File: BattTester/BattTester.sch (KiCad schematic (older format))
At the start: 25 parts, among them J1 Battery, J2 SD_Card, J3 PWR, J4 UPDI, Q1 IRLZ44N, U1 LTC1286CN8, U2 ATtiny1624-SS, U3 LD1086DT33, U4 LM358AN

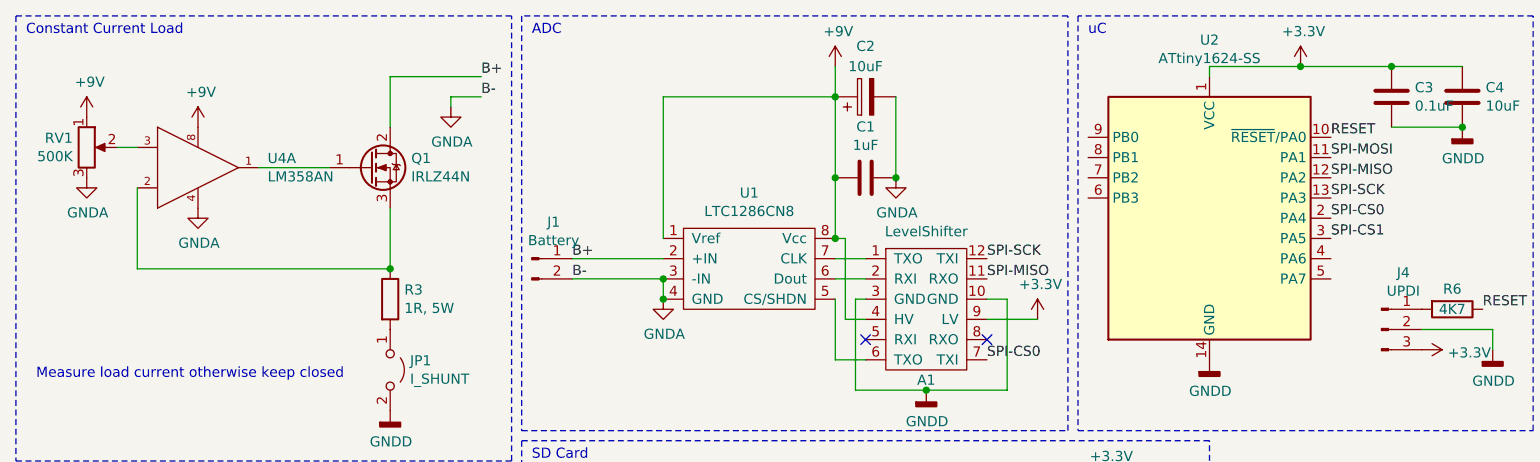
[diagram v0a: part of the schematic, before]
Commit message: cutoff mosfet and higher power Rload
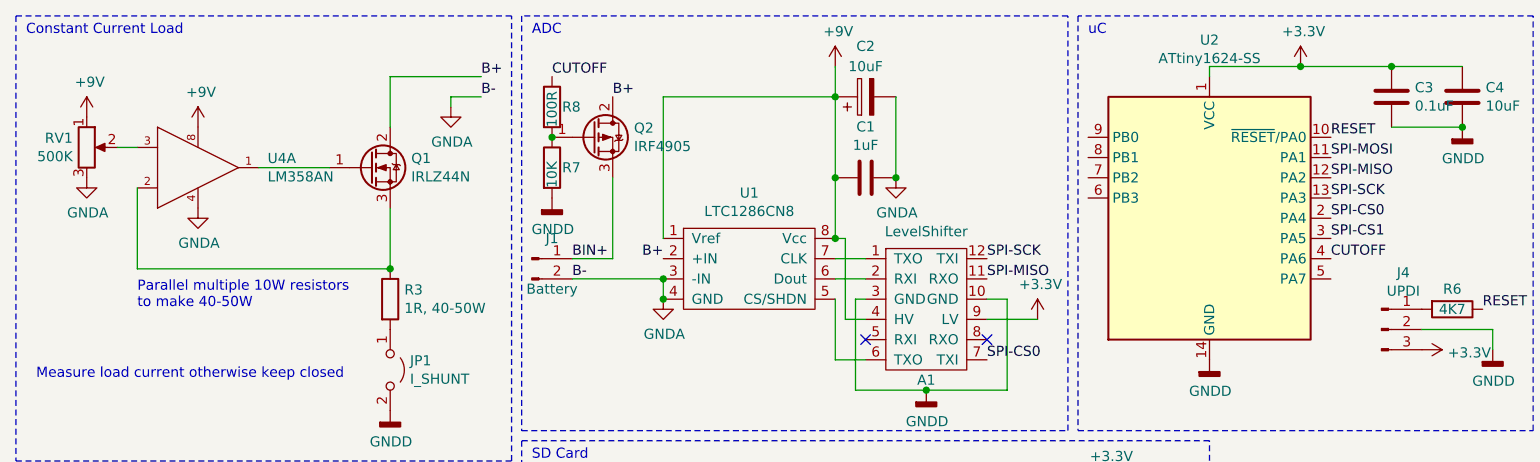
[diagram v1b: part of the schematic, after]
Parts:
- added Q2: IRF4905, Package_TO_SOT_THT:TO-220-3_Vertical, symbol Transistor_FET:IRF4905
- added R7: 10K, Resistor_SMD:R_1206_3216Metric_Pad1.30x1.75mm_HandSolder, symbol Device:R
- added R8: 100R, Resistor_SMD:R_1206_3216Metric_Pad1.30x1.75mm_HandSolder, symbol Device:R
- R3: value 1R, 5W -> 1R, 40-50W; footprint Resistor_THT:R_Axial_Power_L48.0mm_W12.5mm_P55.88mm -> BattTester:10xParallel_R_Axial_DIN0614_L14.3mm_D5.7mm_P15.24mm_Horizontal
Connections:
- net B+: now also Q2.2 (D); no longer J1.1 (Pin_1)
- net GND: now also R7.2
- net CUTOFF: now reaches U2.4 (PA6)
- net CUTOFF: now also R8.1
- new net: Q2.1 (G), R7.1, R8.2
- new net BIN+: J1.1 (Pin_1), Q2.3 (S)
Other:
- note added: "Parallel multiple 10W resistors \nto make 40-50W\n"
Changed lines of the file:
@@
 U 1 1 616C4F2E
 P 3050 1700
-F 0 "J1" H 3158 1881 50  0000 C CNN
-F 1 "Battery" H 3158 1790 50  0000 C CNN
+F 0 "J1" H 3150 1800 50  0000 C CNN
+F 1 "Battery" H 3150 1550 50  0000 C CNN
 F 2 "Connector_PinHeader_2.54mm:PinHeader_1x02_P2.54mm_Vertical" H 3050 1700 50  0001 C CNN
 F 3 "~" H 3050 1700 50  0001 C CNN
 	1    3050 1700
-	1    0    0    -1
-$EndComp
-$Comp
-L power:GNDA #PWR0101
-U 1 1 616C6E3A
-P 3700 1900
-F 0 "#PWR0101" H 3700 1650 50  0001 C CNN
-F 1 "GNDA" H 3705 1727 50  0000 C CNN
-F 2 "" H 3700 1900 50  0001 C CNN
-F 3 "" H 3700 1900 50  0001 C CNN
-	1    3700 1900
 	1    0    0    -1
 $EndComp
@@
 	1100 1350 1100 1750
 Wire Wire Line
-	1100 1750 2350 1750
-Wire Wire Line
 	2350 1450 2350 1750
-$Comp
-L Device:R R3
-U 1 1 6173721B
-P 2350 1900
-F 0 "R3" H 2420 1946 50  0000 L CNN
-F 1 "1R, 5W" H 2420 1855 50  0000 L CNN
-F 2 "Resistor_THT:R_Axial_Power_L48.0mm_W12.5mm_P55.88mm" V 2280 1900 50  0001 C CNN
-F 3 "~" H 2350 1900 50  0001 C CNN
-	1    2350 1900
-	1    0    0    -1
-$EndComp
-Connection ~ 2350 1750
 Wire Wire Line
 	2350 1050 2350 800
@@
 Text Label 2800 800  0    50   ~ 0
 B+
-Connection ~ 3700 1900
 Text Label 3250 1800 0    50   ~ 0
 B-
-Text Label 3250 1700 0    50   ~ 0
-B+
 Text Label 2800 900  0    50   ~ 0
 B-
 Wire Wire Line
-	2800 900  2650 900
-Wire Wire Line
-	2650 900  2650 950
-$Comp
-L power:GNDA #PWR0123
-U 1 1 61740EA0
-P 2650 950
-F 0 "#PWR0123" H 2650 700 50  0001 C CNN
-F 1 "GNDA" H 2655 777 50  0000 C CNN
-F 2 "" H 2650 950 50  0001 C CNN
-F 3 "" H 2650 950 50  0001 C CNN
-	1    2650 950
-	1    0    0    -1
-$EndComp
-Wire Wire Line
 	1000 1150 1100 1150
-Wire Wire Line
-	3250 1700 3700 1700
 $Comp
 L BattTester:LT1286CN8 U1
@@
 Wire Wire Line
 	1150 4300 850  4300
-$Comp
-L power:GNDD #PWR0122
-U 1 1 6178CCE3
+Wire Wire Line
+	7800 2050 7450 2050
+Text Label 3700 1700 2    50   ~ 0
+B+
+Connection ~ 3700 1800
+$Comp
+L power:GNDA #PWR0101
+U 1 1 616C6E3A
+P 3700 1900
+F 0 "#PWR0101" H 3700 1650 50  0001 C CNN
+F 1 "GNDA" H 3705 1727 50  0000 C CNN
+F 2 "" H 3700 1900 50  0001 C CNN
+F 3 "" H 3700 1900 50  0001 C CNN
+	1    3700 1900
+	1    0    0    -1
+$EndComp
+Connection ~ 3700 1900
+Wire Wire Line
+	3250 1800 3700 1800
+Wire Wire Line
+	2800 900  2650 900
+Wire Wire Line
+	2650 900  2650 950
+$Comp
+L power:GNDA #PWR0122
+U 1 1 6171593F
+P 2650 950
+F 0 "#PWR0122" H 2650 700 50  0001 C CNN
+F 1 "GNDA" H 2655 777 50  0000 C CNN
+F 2 "" H 2650 950 50  0001 C CNN
+F 3 "" H 2650 950 50  0001 C CNN
+	1    2650 950
+	1    0    0    -1
+$EndComp
+$Comp
+L power:GNDD #PWR0123
+U 1 1 61715D3B
 P 2350 2450
-F 0 "#PWR0122" H 2350 2200 50  0001 C CNN
+F 0 "#PWR0123" H 2350 2200 50  0001 C CNN
 F 1 "GNDD" H 2354 2295 50  0000 C CNN
 F 2 "" H 2350 2450 50  0001 C CNN
@@
 	1    0    0    -1
 $EndComp
-Wire Wire Line
-	7800 2050 7450 2050
-Connection ~ 3700 1800
-Wire Wire Line
-	3250 1800 3700 1800
+$Comp
+L Transistor_FET:IRF4905 Q2
+U 1 1 616DBDAF
+P 3350 1100
+F 0 "Q2" H 3555 1146 50  0000 L CNN
+F 1 "IRF4905" H 3555 1055 50  0000 L CNN
+F 2 "Package_TO_SOT_THT:TO-220-3_Vertical" H 3550 1025 50  0001 L CIN
+F 3 "http://www.infineon.com/dgdl/irf4905.pdf?fileId=5546d462533600a4015355e32165197c" H 3350 1100 50  0001 L CNN
+	1    3350 1100
+	1    0    0    -1
+$EndComp
+Text Label 3450 900  0    50   ~ 0
+B+
+Text Label 3150 800  0    50   ~ 0
+CUTOFF
+Text Label 3250 1700 0    50   ~ 0
+BIN+
+Wire Wire Line
+	3450 1700 3450 1300
+Wire Wire Line
+	3250 1700 3450 1700
+$Comp
+L Device:R R8
+U 1 1 616FC2A8
+P 3150 950
+F 0 "R8" H 3200 950 50  0000 L CNN
+F 1 "100R" V 3150 850 50  0000 L CNN
+F 2 "Resistor_SMD:R_1206_3216Metric_Pad1.30x1.75mm_HandSolder" V 3080 950 50  0001 C CNN
+F 3 "~" H 3150 950 50  0001 C CNN
+	1    3150 950
+	1    0    0    -1
+$EndComp
+$Comp
+L Device:R R7
+U 1 1 616FD045
+P 3150 1250
+F 0 "R7" H 3200 1250 50  0000 L CNN
+F 1 "10K" V 3150 1150 50  0000 L CNN
+F 2 "Resistor_SMD:R_1206_3216Metric_Pad1.30x1.75mm_HandSolder" V 3080 1250 50  0001 C CNN
+F 3 "~" H 3150 1250 50  0001 C CNN
+	1    3150 1250
+	1    0    0    -1
+$EndComp
+Connection ~ 3150 1100
+$Comp
+L power:GNDD #PWR0126
+U 1 1 616FFF6B
+P 3150 1400
+F 0 "#PWR0126" H 3150 1150 50  0001 C CNN
+F 1 "GNDD" H 3154 1245 50  0000 C CNN
+F 2 "" H 3150 1400 50  0001 C CNN
+F 3 "" H 3150 1400 50  0001 C CNN
+	1    3150 1400
+	1    0    0    -1
+$EndComp
+Text Label 7000 1700 0    50   ~ 0
+CUTOFF
+Connection ~ 2350 1750
+Wire Wire Line
+	1100 1750 2350 1750
+$Comp
+L Device:R R3
+U 1 1 6173721B
+P 2350 1900
+F 0 "R3" H 2420 1946 50  0000 L CNN
+F 1 "1R, 40-50W" H 2420 1855 50  0000 L CNN
+F 2 "BattTester:10xParallel_R_Axial_DIN0614_L14.3mm_D5.7mm_P15.24mm_Horizontal" V 2280 1900 50  0001 C CNN
+F 3 "~" H 2350 1900 50  0001 C CNN
+	1    2350 1900
+	1    0    0    -1
+$EndComp
+Text Notes 1100 1950 0    50   ~ 0
+Parallel multiple 10W resistors \nto make 40-50W\n
 $EndSCHEMATC

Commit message: Fix #1
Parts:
- added Q3: 2N7002, Package_TO_SOT_SMD:SOT-23, symbol Transistor_FET:2N7002
- added R9: 10K, Resistor_SMD:R_1206_3216Metric_Pad1.30x1.75mm_HandSolder, symbol Device:R
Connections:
- net BIN+: now also R7.2
- net GND: now also Q3.2 (S), R9.2; no longer R7.2
- net at Q2.1 (G), R7.1: now also Q3.3 (D); no longer R8.2
- new net: Q3.1 (G), R8.2, R9.1
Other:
- moved on the sheet: A1, C1, C2, C3, C4, J1, J4, Q2, R6, R7, R8, U1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

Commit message: current check
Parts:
- added R?: 10m, symbol Device:R
- added R?: 100R, symbol Device:R
- added R?: 2K, symbol Device:R
- added U?: LT6106, Package_TO_SOT_SMD:SOT-23-5, symbol Amplifier_Current:LT6106
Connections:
- net GND: now also R?.2, U?.2 (V-)
- new net: R?.1, U?.3 (-)
- new net: R?.2, U?.4 (+)
- new net: R?.1, R?.2, U?.5 (V+)
- new net I_OUT: R?.1, U?.1
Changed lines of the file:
@@
 	1    0    0    -1
 $EndComp
-Text Label 3300 1700 0    50   ~ 0
-BIN+
 Text Label 3900 800  0    50   ~ 0
 CUTOFF
@@
 Text Label 4200 1700 2    50   ~ 0
 B+
+$Comp
+L Amplifier_Current:LT6106 U?
+U 1 1 61967F7F
+P 7800 3400
+F 0 "U?" H 8144 3446 50  0000 L CNN
+F 1 "LT6106" H 8144 3355 50  0000 L CNN
+F 2 "Package_TO_SOT_SMD:SOT-23-5" H 7800 3400 50  0001 C CNN
+F 3 "https://www.analog.com/media/en/technical-documentation/data-sheets/6106fb.pdf" H 7850 3600 50  0001 C CNN
+	1    7800 3400
+	1    0    0    -1
+$EndComp
+$Comp
+L Device:R R?
+U 1 1 6196A136
+P 6900 3400
+F 0 "R?" H 6950 3400 50  0000 L CNN
+F 1 "10m" V 6900 3300 50  0000 L CNN
+F 2 "" V 6830 3400 50  0001 C CNN
+F 3 "~" H 6900 3400 50  0001 C CNN
+	1    6900 3400
+	1    0    0    -1
+$EndComp
+$Comp
+L Device:R R?
+U 1 1 6196AB0E
+P 7150 3250
+F 0 "R?" V 7050 3250 50  0000 C CNN
+F 1 "100R" V 7150 3250 50  0000 C CNN
+F 2 "" V 7080 3250 50  0001 C CNN
+F 3 "~" H 7150 3250 50  0001 C CNN
+	1    7150 3250
+	0    1    1    0
+$EndComp
+$Comp
+L Device:R R?
+U 1 1 6196BAA8
+P 8100 3550
+F 0 "R?" H 8150 3550 50  0000 L CNN
+F 1 "2K" V 8100 3500 50  0000 L CNN
+F 2 "" V 8030 3550 50  0001 C CNN
+F 3 "~" H 8100 3550 50  0001 C CNN
+	1    8100 3550
+	1    0    0    -1
+$EndComp
+Wire Wire Line
+	6900 3250 7000 3250
+Wire Wire Line
+	6900 3550 7300 3550
+Wire Wire Line
+	7300 3250 7500 3500
+Wire Wire Line
+	7300 3550 7500 3300
+Wire Wire Line
+	7700 3100 6900 3100
+Wire Wire Line
+	6900 3100 6900 3250
+Connection ~ 6900 3250
+$Comp
+L power:GNDD #PWR?
+U 1 1 61978BAC
+P 7700 3700
+F 0 "#PWR?" H 7700 3450 50  0001 C CNN
+F 1 "GNDD" H 7704 3545 50  0000 C CNN
+F 2 "" H 7700 3700 50  0001 C CNN
+F 3 "" H 7700 3700 50  0001 C CNN
+	1    7700 3700
+	1    0    0    -1
+$EndComp
+Wire Wire Line
+	7700 3700 8100 3700
+Connection ~ 7700 3700
+Text Label 8350 3400 0    50   ~ 0
+I_OUT
+Wire Wire Line
+	8100 3400 8350 3400
+Connection ~ 8100 3400
+Text Label 3300 1700 0    50   ~ 0
+BIN+
 $EndSCHEMATC

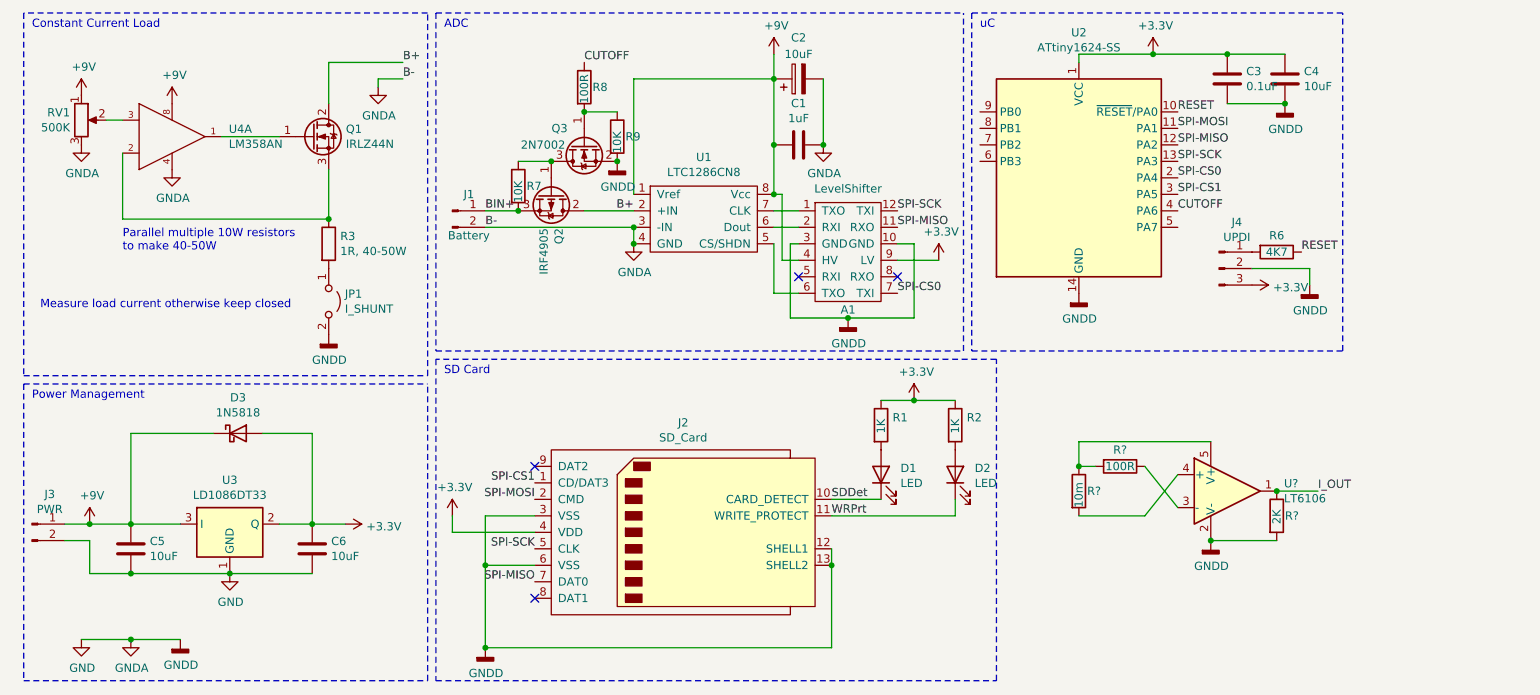
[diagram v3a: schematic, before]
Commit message: add current sense
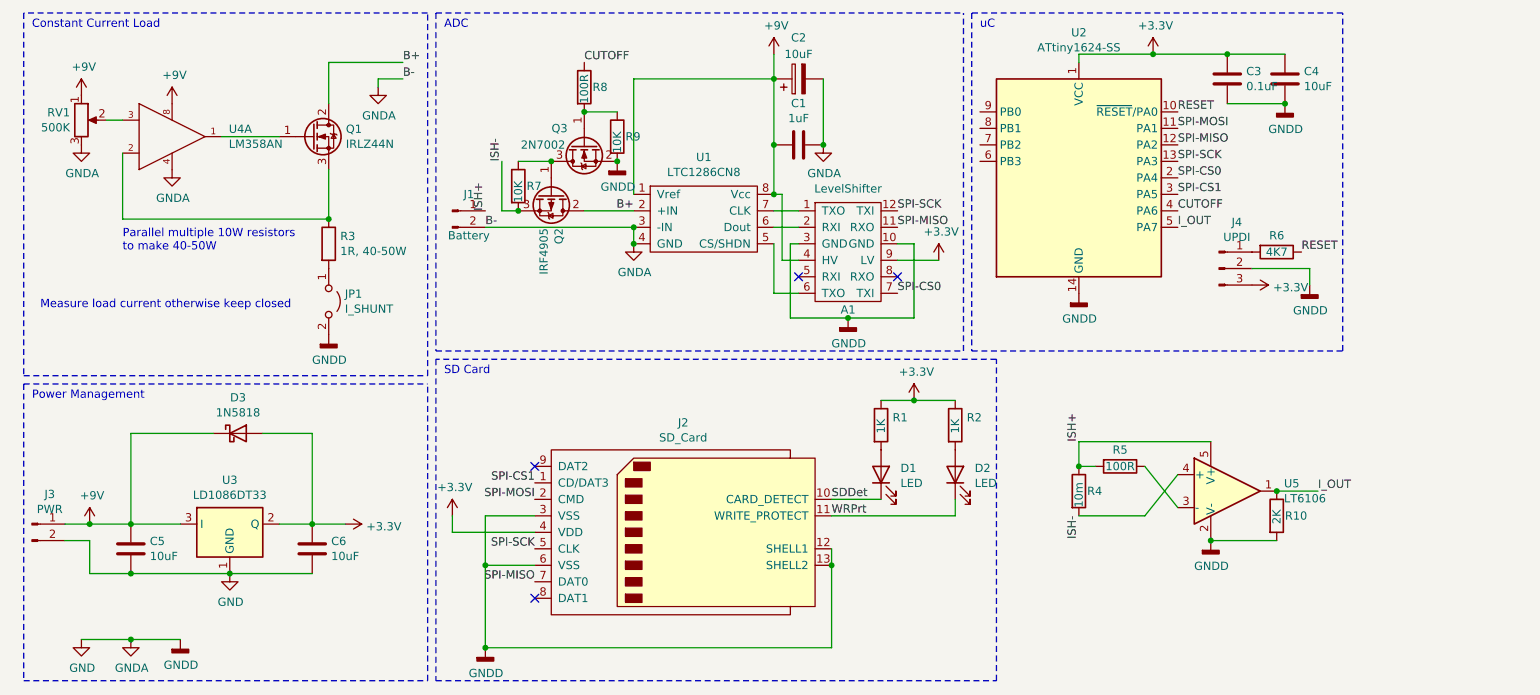
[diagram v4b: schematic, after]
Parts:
- R10, R5: renamed from R?; footprint (none) -> Resistor_SMD:R_0805_2012Metric_Pad1.20x1.40mm_HandSolder
- R4: renamed from R?; footprint (none) -> Resistor_SMD:R_2816_7142Metric_Pad3.20x4.45mm_HandSolder
- gave numbers to parts that had none: 1
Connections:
- net I_OUT: now also U2.5 (PA7)
- net ISH-: now reaches R4.2, U5.4 (+)
- net ISH-: now also Q2.3 (S), R7.2
- net ISH+: now reaches R4.1, R5.2, U5.5 (V+)
- net ISH+: now also J1.1 (Pin_1)
- removed net BIN+: J1.1 (Pin_1), Q2.3 (S), R7.2
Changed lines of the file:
@@
 	1    0    0    -1
 $EndComp
-Wire Wire Line
-	3300 1700 3500 1700
 Text Label 7500 1700 0    50   ~ 0
 CUTOFF
@@
 Wire Wire Line
 	3900 1700 4200 1700
-Connection ~ 3500 1700
 Connection ~ 3900 1100
 Wire Wire Line
@@
 B+
 $Comp
-L Amplifier_Current:LT6106 U?
+L Amplifier_Current:LT6106 U5
 U 1 1 61967F7F
 P 7800 3400
-F 0 "U?" H 8144 3446 50  0000 L CNN
+F 0 "U5" H 8144 3446 50  0000 L CNN
 F 1 "LT6106" H 8144 3355 50  0000 L CNN
 F 2 "Package_TO_SOT_SMD:SOT-23-5" H 7800 3400 50  0001 C CNN
@@
 $EndComp
 $Comp
-L Device:R R?
+L Device:R R4
 U 1 1 6196A136
 P 6900 3400
-F 0 "R?" H 6950 3400 50  0000 L CNN
+F 0 "R4" H 6950 3400 50  0000 L CNN
 F 1 "10m" V 6900 3300 50  0000 L CNN
-F 2 "" V 6830 3400 50  0001 C CNN
+F 2 "Resistor_SMD:R_2816_7142Metric_Pad3.20x4.45mm_HandSolder" V 6830 3400 50  0001 C CNN
 F 3 "~" H 6900 3400 50  0001 C CNN
 	1    6900 3400
@@
 $EndComp
 $Comp
-L Device:R R?
+L Device:R R5
 U 1 1 6196AB0E
 P 7150 3250
-F 0 "R?" V 7050 3250 50  0000 C CNN
+F 0 "R5" V 7050 3250 50  0000 C CNN
 F 1 "100R" V 7150 3250 50  0000 C CNN
-F 2 "" V 7080 3250 50  0001 C CNN
+F 2 "Resistor_SMD:R_0805_2012Metric_Pad1.20x1.40mm_HandSolder" V 7080 3250 50  0001 C CNN
 F 3 "~" H 7150 3250 50  0001 C CNN
 	1    7150 3250
@@
 $EndComp
 $Comp
-L Device:R R?
+L Device:R R10
 U 1 1 6196BAA8
 P 8100 3550
-F 0 "R?" H 8150 3550 50  0000 L CNN
+F 0 "R10" H 8150 3550 50  0000 L CNN
 F 1 "2K" V 8100 3500 50  0000 L CNN
-F 2 "" V 8030 3550 50  0001 C CNN
+F 2 "Resistor_SMD:R_0805_2012Metric_Pad1.20x1.40mm_HandSolder" V 8030 3550 50  0001 C CNN
 F 3 "~" H 8100 3550 50  0001 C CNN
 	1    8100 3550
@@
 Connection ~ 6900 3250
 $Comp
-L power:GNDD #PWR?
+L power:GNDD #PWR01
 U 1 1 61978BAC
 P 7700 3700
-F 0 "#PWR?" H 7700 3450 50  0001 C CNN
+F 0 "#PWR01" H 7700 3450 50  0001 C CNN
 F 1 "GNDD" H 7704 3545 50  0000 C CNN
 F 2 "" H 7700 3700 50  0001 C CNN
@@
 	8100 3400 8350 3400
 Connection ~ 8100 3400
-Text Label 3300 1700 0    50   ~ 0
-BIN+
+Text Label 3300 1700 1    50   ~ 0
+ISH+
+Wire Wire Line
+	3500 1700 3400 1700
+Wire Wire Line
+	3400 1700 3400 1400
+Connection ~ 3500 1700
+Text Label 3400 1400 1    50   ~ 0
+ISH-
+Text Label 6900 3100 1    50   ~ 0
+ISH+
+Text Label 6900 3550 3    50   ~ 0
+ISH-
+Text Label 7500 1800 0    50   ~ 0
+I_OUT
 $EndSCHEMATC

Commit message: finished routing
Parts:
- removed U3: LD1086DT33, Package_TO_SOT_SMD:TO-252-3_TabPin2, symbol Regulator_Linear:IFX27001TFV33
- added U3: LM1117-3.3, Package_TO_SOT_THT:TO-220-3_Vertical, symbol Regulator_Linear:LM1117-3.3
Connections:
- net +3V3: now also U3.2 (VO)
- net +9V: now also U3.3 (VI)
- net GND: now also U3.1 (GND)
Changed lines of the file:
@@
-$EndComp
-$Comp
-L Regulator_Linear:IFX27001TFV33 U3
-U 1 1 616F6C6D
-P 1750 3600
-F 0 "U3" H 1750 3867 50  0000 C CNN
-F 1 "LD1086DT33" H 1750 3776 50  0000 C CNN
-F 2 "Package_TO_SOT_SMD:TO-252-3_TabPin2" H 1750 3550 50  0001 C CNN
-F 3 "https://static6.arrow.com/aropdfconversion/dc75757ae45a88e5f69bdce3f2a651a5fe0ca07d/ifx27001_ds_10.pdf" H 1750 3550 50  0001 C CNN
-	1    1750 3600
-	1    0    0    -1
 $EndComp
 $Comp
@@
 Text Label 7500 1800 0    50   ~ 0
 I_OUT
+$Comp
+L Regulator_Linear:LM1117-3.3 U3
+U 1 1 619E8D3F
+P 1750 3600
+F 0 "U3" H 1750 3842 50  0000 C CNN
+F 1 "LM1117-3.3" H 1750 3751 50  0000 C CNN
+F 2 "Package_TO_SOT_THT:TO-220-3_Vertical" H 1750 3600 50  0001 C CNN
+F 3 "http://www.ti.com/lit/ds/symlink/lm1117.pdf" H 1750 3600 50  0001 C CNN
+	1    1750 3600
+	1    0    0    -1
+$EndComp
 $EndSCHEMATC

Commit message: add test point
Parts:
- added TP1: Current measurement, Connector_PinHeader_2.54mm:PinHeader_1x02_P2.54mm_Vertical, symbol Connector:TestPoint_2Pole
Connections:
- net GND: now also TP1.2
- net I_OUT: now also TP1.1
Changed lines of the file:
@@
 	7700 3700 8100 3700
 Connection ~ 7700 3700
-Text Label 8350 3400 0    50   ~ 0
+Text Label 8600 3400 0    50   ~ 0
 I_OUT
-Wire Wire Line
-	8100 3400 8350 3400
 Connection ~ 8100 3400
 Text Label 3300 1700 1    50   ~ 0
@@
 	1    0    0    -1
 $EndComp
+$Comp
+L Connector:TestPoint_2Pole TP1
+U 1 1 619EDCE6
+P 8600 3600
+F 0 "TP1" V 8554 3658 50  0000 L CNN
+F 1 "Current measurement" V 8645 3658 50  0000 L CNN
+F 2 "Connector_PinHeader_2.54mm:PinHeader_1x02_P2.54mm_Vertical" H 8600 3600 50  0001 C CNN
+F 3 "~" H 8600 3600 50  0001 C CNN
+	1    8600 3600
+	0    1    1    0
+$EndComp
+Wire Wire Line
+	8100 3400 8600 3400
+Wire Wire Line
+	8600 3800 8100 3800
+Wire Wire Line
+	8100 3800 8100 3700
+Connection ~ 8100 3700
 $EndSCHEMATC
